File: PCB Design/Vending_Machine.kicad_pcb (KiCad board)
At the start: 2 copper layers, 116.6 x 143.7 mm, 178 parts, among them J1 Mains, J11 Conn_Aux, J12 Conn_Sig, J13 Conn_I2C, J14 Conn_I2C, J2 Conn_IO, J3 Conn_IO11, J31 GPIO5, J32 GPIO3, J33 GPIO2, J34 GPIO4, J35 Conn_01x15, J36 UART0, J37 Display, J38 Conn_01x15, J39 GPIO1, J4 Conn_IO12, J40 I2C, J42 Conn, J43 Conn_I2C, J46 Conn_I2C, J47 Conn_Sig, J48 I2C, SW31 EN, SW32 BOOT, U11 AMS1117-3.3, U12 SX1509BIULTRT, U13 TCA9406DC, U31 AMS1117-3.3, U32 TCA9406DC, U33 ESP32-WROOM-32UE, U41 AMS1117-3.3, U42 SX1509BIULTRT, U43 TCA9406DC

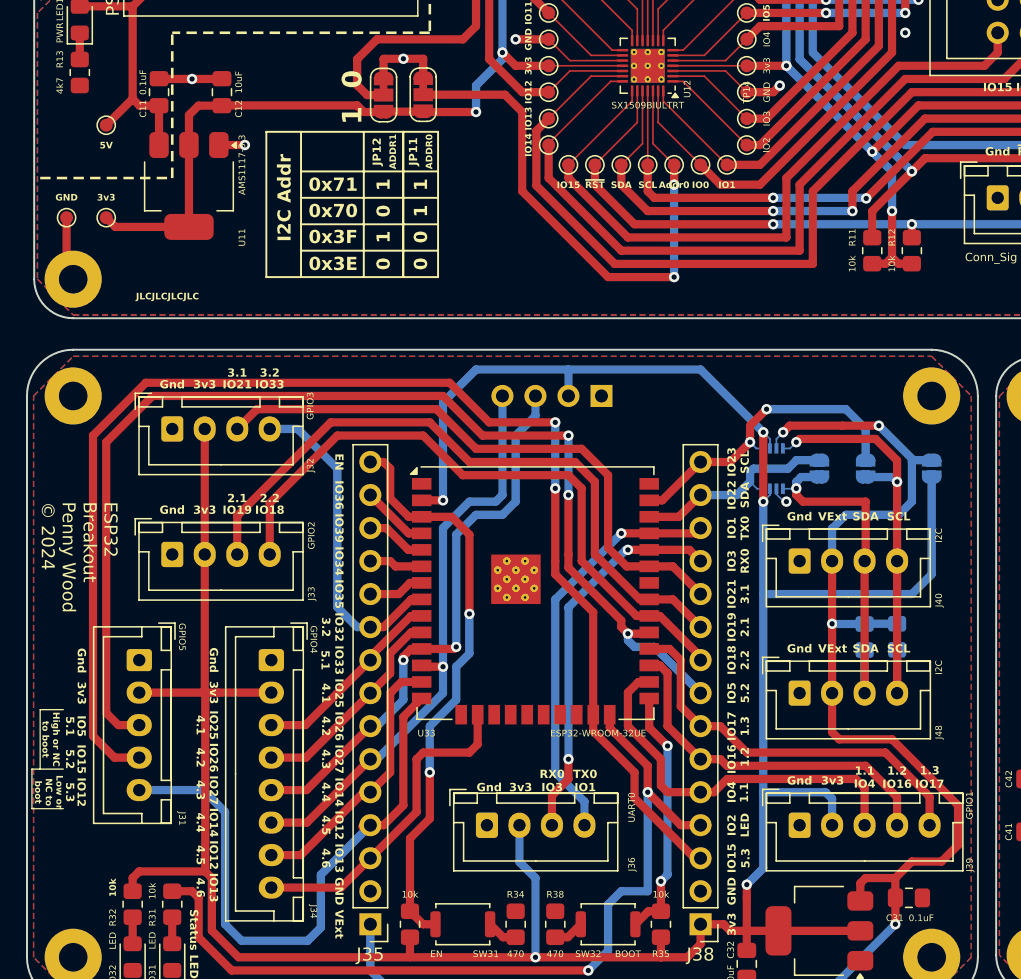
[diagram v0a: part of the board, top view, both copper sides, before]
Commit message: Fixed silk screens
Silk screen had incorrect numbering for some pins.
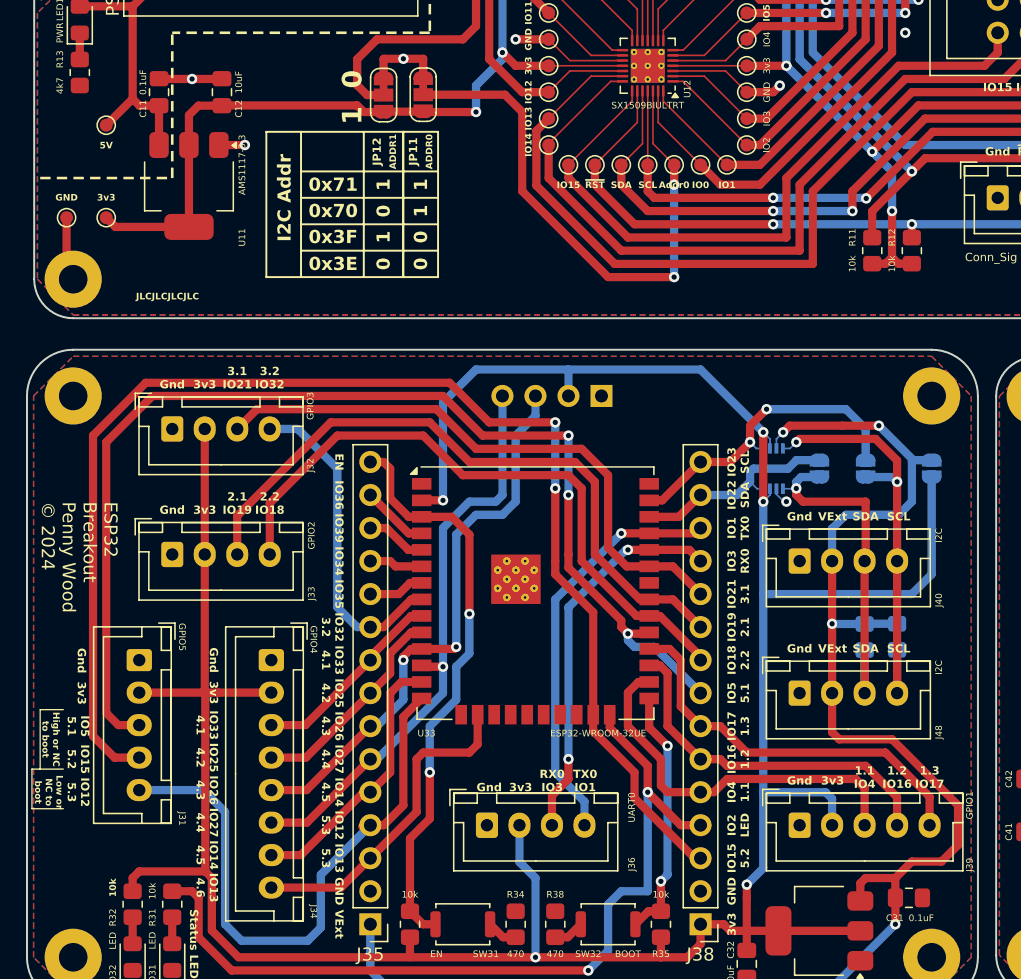
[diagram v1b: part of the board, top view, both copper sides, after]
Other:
- board text added: "1.1 IO4"
- board text added: "1.2 IO16"
- board text added: "1.3 IO17"
- board text added: "2.1 IO19"
- board text added: "2.2 IO18"
- board text added: "3.1 IO21"
- board text added: "3.2 IO32"
- board text added: "IO1 TX0"
- board text added: "IO12 5.3"
- board text added: "IO13 4.6"
- board text added: "IO13 5.3"
- board text added: "IO14 4.5"
- board text added: "IO15 5.2"
- board text added: "IO16 1.2"
- board text added: "IO17 1.3"
- board text added: "IO18 2.2"
- board text added: "IO19 2.1"
- board text added: "IO21 3.1"
- board text added: "IO22 SDA"
- board text added: "IO23 SCL"
- board text added: "IO25 4.2"
- board text added: "IO26 4.3"
- board text added: "IO27 4.4"
- board text added: "IO3 RX0"
- board text added: "IO32 3.2"
- board text added: "IO33 4.1"
- board text added: "IO4 1.1"
- board text added: "IO5 5.1"
- board text removed: "1.1"
- board text removed: "1.2"
- board text removed: "1.3"
- board text removed: "2.1"
- board text removed: "2.2"
- board text removed: "3.1"
- board text removed: "3.2"
- board text removed: "4.1"
- board text removed: "4.2"
- board text removed: "4.3"
- board text removed: "4.4"
- board text removed: "4.5"
- board text removed: "4.6"
- board text removed: "5.1"
- board text removed: "5.2"
- board text removed: "5.3"
- board text removed: "IO16"
- board text removed: "IO17"
- board text removed: "IO18"
- board text removed: "IO19"
- board text removed: "IO21"
- board text removed: "IO22"
- board text removed: "IO23"
- board text removed: "IO25"
- board text removed: "IO32"
- board text removed: "IO33"
